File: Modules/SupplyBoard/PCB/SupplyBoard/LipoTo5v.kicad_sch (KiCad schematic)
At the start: 0 parts

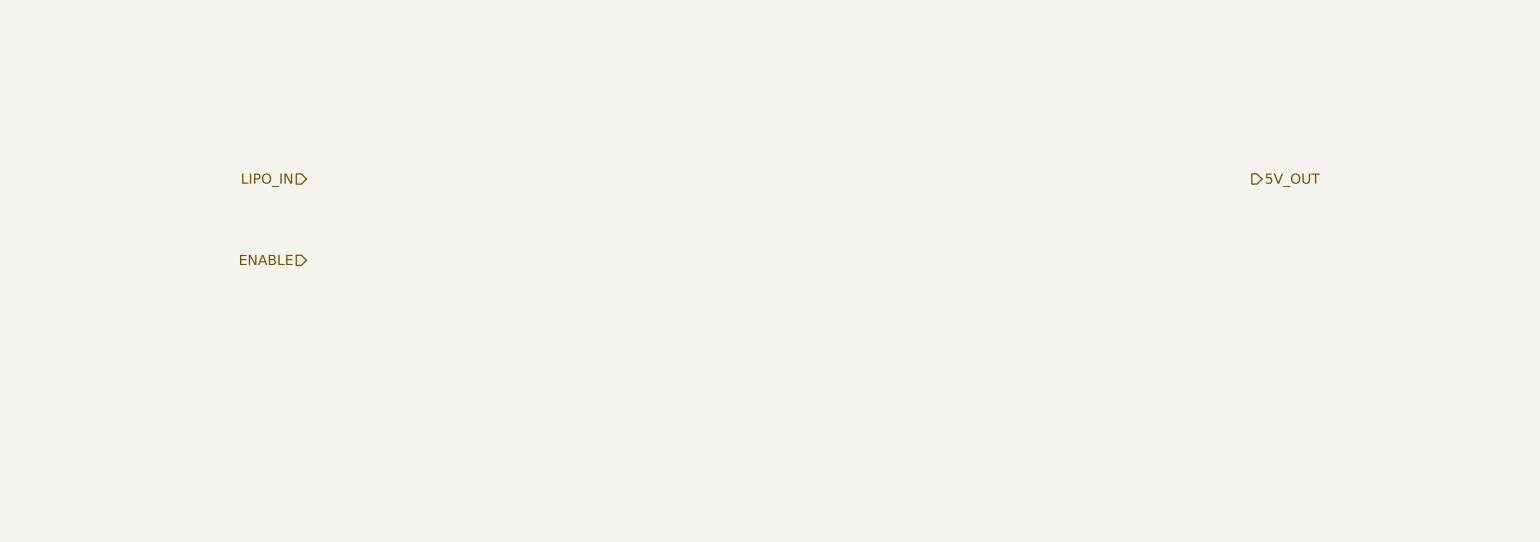
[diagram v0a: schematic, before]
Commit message: Lipo to 3v3 circuit added
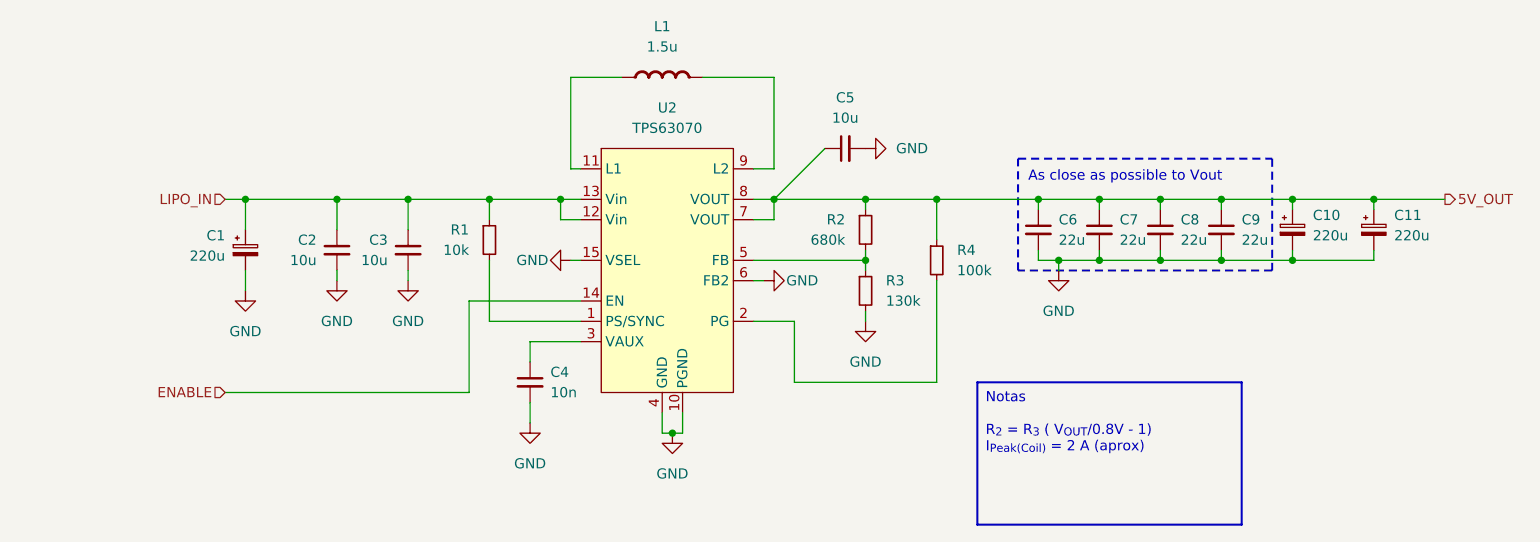
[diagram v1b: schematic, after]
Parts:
- added C1, C10, C11: 220u, Capacitor_SMD:CP_Elec_6.3x5.4, symbol Device:C_Polarized_Small
- added C2, C3, C5: 10u, Capacitor_SMD:C_0805_2012Metric_Pad1.18x1.45mm_HandSolder, symbol Device:C_Small
- added C4: 10n, Capacitor_SMD:C_0805_2012Metric_Pad1.18x1.45mm_HandSolder, symbol Device:C_Small
- added C6, C7, C8, C9: 22u, Capacitor_SMD:C_0805_2012Metric_Pad1.18x1.45mm_HandSolder, symbol Device:C_Small
- added L1: 1.5u, Inductor_SMD:L_Coilcraft_XxL4040, symbol PCM_Elektuur:L
- added R1: 10k, symbol Device:R_Small
- added R2: 680k, symbol Device:R_Small
- added R3: 130k, symbol Device:R_Small
- added R4: 100k, symbol Device:R_Small
- added U2: TPS63070, IcaroFootprints:RNM0015A, symbol IcaroLib:TPS63070RNMR
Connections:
- net 5V_OUT: now also C10.1, C11.1, C5.1, C6.1, C7.1, C8.1, C9.1, R2.1, R4.1, U2.7 (VOUT), U2.8 (VOUT)
- net ENABLE: now also U2.14 (EN)
- net LIPO_IN: now also C1.1, C2.1, C3.1, R1.1, U2.12 (Vin), U2.13 (Vin)
- new net: R1.2, U2.1 (PS/SYNC)
- new net: L1.1 (+), U2.11 (L1)
- new net: R4.2, U2.2 (PG)
- new net: C4.1, U2.3 (VAUX)
- new net: R2.2, R3.1, U2.5 (FB)
- new net: L1.2 (-), U2.9 (L2)
- new net GND: C1.2, C10.2, C11.2, C2.2, C3.2, C4.2, C5.2, C6.2, C7.2, C8.2, C9.2, R3.2, U2.10 (PGND), U2.15 (VSEL), U2.4 (GND), U2.6 (FB2)
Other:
- note added: "As close as possible to Vout"

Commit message: SupplyBoard - Added INA2180 current sensor
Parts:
- added FB1: FerriteBead, symbol Device:FerriteBead
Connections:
- net LIPO_IN: now also FB1.1; no longer C1.1, C2.1, C3.1, R1.1, U2.12 (Vin), U2.13 (Vin)
- new net: C1.1, C2.1, C3.1, FB1.2, R1.1, U2.12 (Vin), U2.13 (Vin)
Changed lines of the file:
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@@
+	)
+	(junction
+		(at 71.12 69.85)
+		(diameter 0)
+		(color 0 0 0 0)
 	)
 	(junction
@@
 	)
 	(junction
-		(at 71.12 69.85)
-		(diameter 0)
-		(color 0 0 0 0)
-	)
-	(junction
 		(at 148.59 69.85)
 		(diameter 0)
@@
 	(wire
 		(pts
-			(xy 68.58 69.85) (xy 71.12 69.85)
-		)
-		(stroke
-			(width 0)
-			(type default)
-		)
-	)
-	(wire
-		(pts
 			(xy 91.44 69.85) (xy 91.44 73.66)
 		)
@@
 	(wire
 		(pts
+			(xy 67.31 69.85) (xy 71.12 69.85)
+		)
+		(stroke
+			(width 0)
+			(type default)
+		)
+	)
+	(wire
+		(pts
 			(xy 193.04 76.2) (xy 193.04 77.47)
 		)
@@
 		(pts
 			(xy 101.6 69.85) (xy 101.6 72.39)
+		)
+		(stroke
+			(width 0)
+			(type default)
+		)
+	)
+	(wire
+		(pts
+			(xy 53.34 69.85) (xy 59.69 69.85)
 		)
 		(stroke
@@
 	(hierarchical_label "LIPO_IN"
 		(shape input)
-		(at 68.58 69.85 180)
+		(at 53.34 69.85 180)
 		(effects
 			(font
@@
 					(unit 1)
 				)
+			)
+		)
+	)
+	(symbol
+		(lib_id "Device:FerriteBead")
+		(at 63.5 69.85 90)
+		(unit 1)
+		(exclude_from_sim no)
+		(in_bom yes)
+		(on_board yes)
+		(dnp no)
+		(fields_autoplaced yes)
+		(property "Reference" "FB1"
+			(at 63.4492 62.23 90)
+			(effects
+				(font
+					(size 1.27 1.27)
+				)
+			)
+		)
+		(property "Value" "FerriteBead"
+			(at 63.4492 64.77 90)
+			(effects
+				(font
+					(size 1.27 1.27)
+				)
+			)
+		)
+		(property "Footprint" ""
+			(at 63.5 71.628 90)
+			(effects
+				(font
+					(size 1.27 1.27)
+				)
+				(hide yes)
+			)
+		)
+		(property "Datasheet" "~"
+			(at 63.5 69.85 0)
+			(effects
+				(font
+					(size 1.27 1.27)
+				)
+				(hide yes)
+			)
+		)
+		(property "Description" "Ferrite bead"
+			(at 63.5 69.85 0)
+			(effects
+				(font
+					(size 1.27 1.27)
+				)
+				(hide yes)
+			)
+		)
+		(pin "2"
+		)
+		(pin "1"
+		)
+		(instances
+			(project ""
+				(path "/e0885a0e-6910-46ab-84fb-bbb29c8999bc/51098744-09f0-4457-9943-7f94628fee2f"
+					(reference "FB1")
+					(unit 1)
+				)

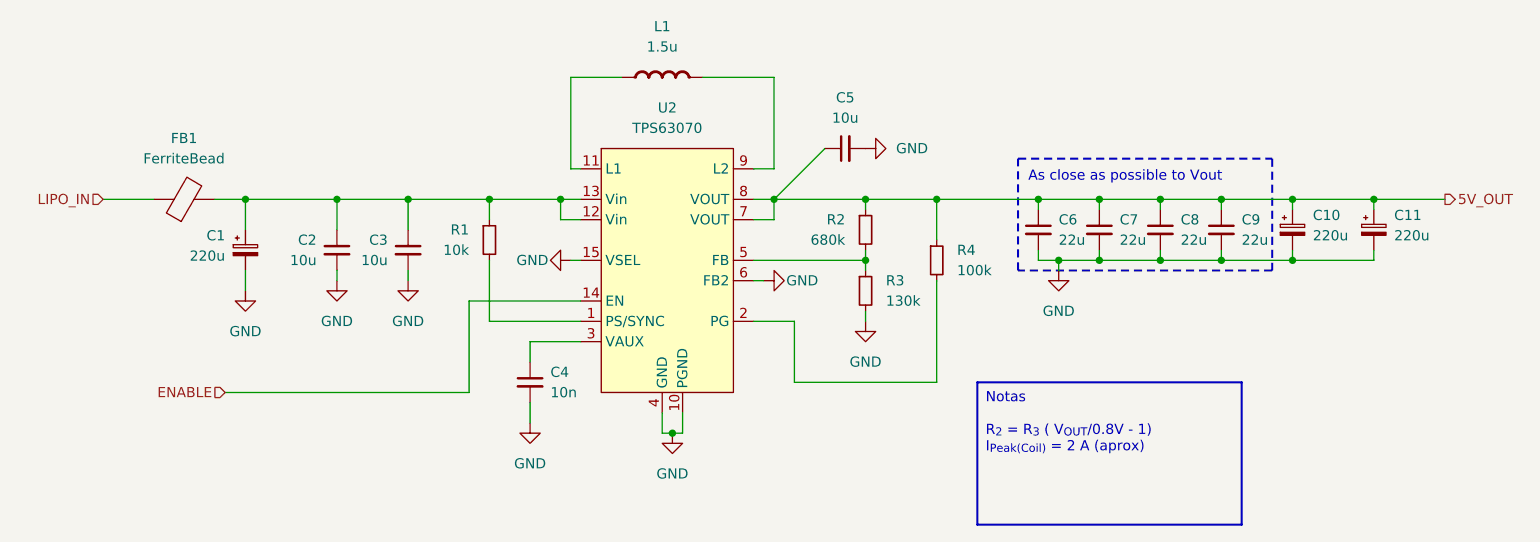
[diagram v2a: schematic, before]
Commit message: Supply board schematic and PCB
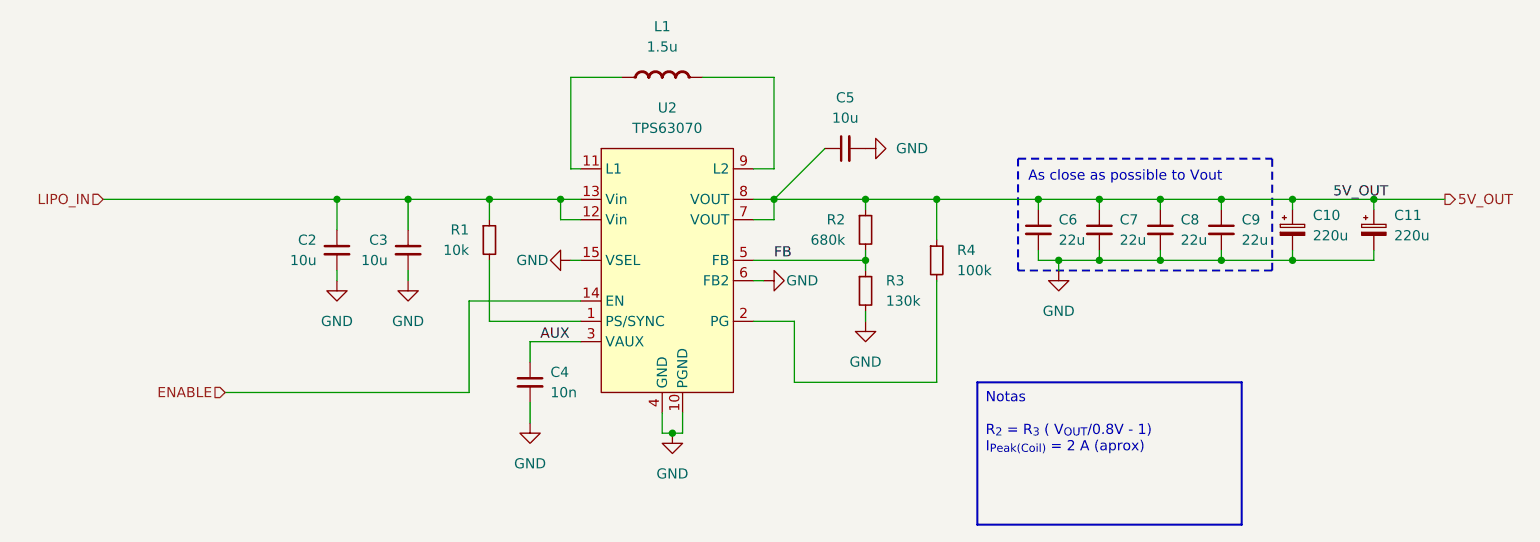
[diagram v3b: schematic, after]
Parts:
- removed C1: 220u, Capacitor_SMD:CP_Elec_6.3x5.4, symbol Device:C_Polarized_Small
- removed FB1: FerriteBead, symbol Device:FerriteBead
- C2, C3, C4, C5, C6, C7, C8, C9: footprint Capacitor_SMD:C_0805_2012Metric_Pad1.18x1.45mm_HandSolder -> Capacitor_SMD:C_0603_1608Metric_Pad1.08x0.95mm_HandSolder
- R1, R2, R3, R4: footprint (none) -> Resistor_SMD:R_0603_1608Metric_Pad0.98x0.95mm_HandSolder
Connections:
- net LIPO_IN: now also C2.1, C3.1, R1.1, U2.12 (Vin), U2.13 (Vin)
- net AUX: now reaches C4.1, U2.3 (VAUX)
- net FB: now reaches R2.2, R3.1, U2.5 (FB)

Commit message: Updated supply board for v2, and BMP280 tinkering project
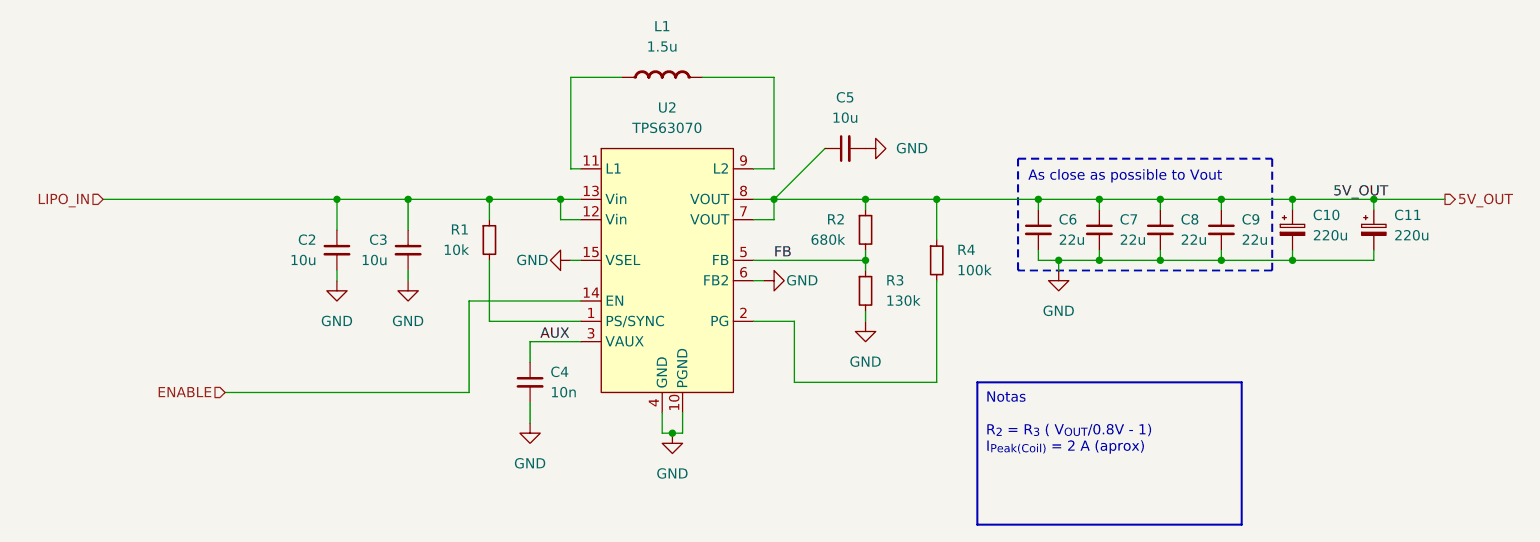
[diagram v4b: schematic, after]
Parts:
- C10, C11: footprint Capacitor_SMD:CP_Elec_6.3x5.4 -> Capacitor_Tantalum_SMD:CP_EIA-3216-18_Kemet-A_Pad1.58x1.35mm_HandSolder

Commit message: Finished Supply board
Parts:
- C10, C11: footprint Capacitor_Tantalum_SMD:CP_EIA-3216-18_Kemet-A_Pad1.58x1.35mm_HandSolder -> Capacitor_Tantalum_SMD:CP_EIA-3528-21_Kemet-B_Pad1.50x2.35mm_HandSolder
- L1: footprint Inductor_SMD:L_Coilcraft_XxL4040 -> Inductor_SMD:L_Cenker_CKCS4030
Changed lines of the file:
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@@
 			)
 		)
-		(property "Footprint" "Capacitor_Tantalum_SMD:CP_EIA-3216-18_Kemet-A_Pad1.58x1.35mm_HandSolder"
+		(property "Footprint" "Capacitor_Tantalum_SMD:CP_EIA-3528-21_Kemet-B_Pad1.50x2.35mm_HandSolder"
 			(at 201.93 73.66 0)
 			(effects
@@
 			)
 		)
-		(property "Footprint" "Inductor_SMD:L_Coilcraft_XxL4040"
+		(property "Footprint" "Inductor_SMD:L_Cenker_CKCS4030"
 			(at 123.19 54.61 0)
 			(effects
@@
 			)
 		)
-		(property "Footprint" "Capacitor_Tantalum_SMD:CP_EIA-3216-18_Kemet-A_Pad1.58x1.35mm_HandSolder"
+		(property "Footprint" "Capacitor_Tantalum_SMD:CP_EIA-3528-21_Kemet-B_Pad1.50x2.35mm_HandSolder"
 			(at 212.09 73.66 0)
 			(effects
